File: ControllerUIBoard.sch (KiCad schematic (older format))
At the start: 17 parts

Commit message: [modified:] uln2003 package swap [modified:] Display nomenclature update
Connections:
- net labels added: KeySwitchA, KeySwitchB
- net labels removed: KeyLock.A, KeyLock.B, KeySwitch.A, KeySwitch.B
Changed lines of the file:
@@
 	4700 4850 6400 4850
 Text Label 6400 4450 0    50   ~ 0
-KeySwitch.A
+KeySwitchA
 Text Label 6400 4550 0    50   ~ 0
-KeySwitch.B
+KeySwitchB
 Text Label 6400 3350 0    50   ~ 0
 Signal_Strength_Dial_+
@@
 	1    0    0    -1
 $EndComp
-Text Label 9850 5400 0    50   ~ 0
-KeyLock.A
-Text Label 9850 5500 0    50   ~ 0
-KeyLock.B
 Wire Wire Line
 	9850 5500 9550 5500
@@
 	8850 3650 8600 3650
 Wire Wire Line
-	8700 3750 8850 3750
-Wire Wire Line
 	8850 3850 8600 3850
 Wire Wire Line
 	9350 3850 9600 3850
-Wire Wire Line
-	9600 3750 9350 3750
 Wire Wire Line
 	9600 3550 9350 3550
@@
 Wire Wire Line
 	9350 3650 10700 3650
-Wire Notes Line
-	7600 1850 7600 6000
 Text Notes 7650 2100 0    50   ~ 0
 Spiegelung um Längsachse nätig, je nach Orientierung
@@
 	1    0    0    -1
 $EndComp
-$Comp
-L power:GND #PWR?
-U 1 1 6205CDDF
-P 8700 4150
-AR Path="/6205CDDF" Ref="#PWR?"  Part="1"
-AR Path="/60F87146/6205CDDF" Ref="#PWR?"  Part="1"
-AR Path="/60F18E7A/6205CDDF" Ref="#PWR?"  Part="1"
-F 0 "#PWR?" H 8700 3900 50  0001 C CNN
-F 1 "GND" H 8705 3977 50  0000 C CNN
-F 2 "" H 8700 4150 50  0001 C CNN
-F 3 "" H 8700 4150 50  0001 C CNN
-	1    8700 4150
-	1    0    0    -1
-$EndComp
-Wire Wire Line
-	8700 3750 8700 4150
 Wire Wire Line
 	8550 4600 8550 4900
 Text Notes 6400 3450 0    50   ~ 0
 PWM Output\n
+Text Label 8600 3750 2    50   ~ 0
+OnSwitchLedCathode
+Wire Wire Line
+	8600 3750 8850 3750
+Wire Wire Line
+	10700 3750 10700 3650
+Wire Wire Line
+	9350 3750 10700 3750
+Connection ~ 10700 3650
+Text Label 9850 5400 0    50   ~ 0
+KeySwitchA
+Text Label 9850 5500 0    50   ~ 0
+KeySwitchB
 $EndSCHEMATC

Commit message: - Display Driving abgeschlossen
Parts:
- gave numbers to parts that had none: 17

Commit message: - ATmega überarbeitet - Alle offenen Punkte zusammengefasst
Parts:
- removed C38, C39: 100n, Capacitor_SMD:C_0603_1608Metric, symbol Device:C
- removed J1: ATMEGA_ICSP, Connector_PinHeader_2.54mm:PinHeader_2x03_P2.54mm_Vertical, symbol Connector_Generic:Conn_02x03_Odd_Even
- removed J2: Conn_02x01, Connector_PinHeader_2.54mm:PinHeader_1x02_P2.54mm_Vertical, symbol Connector_Generic:Conn_02x01
- removed J9: Conn_01x03_Male, Connector_PinHeader_2.54mm:PinHeader_1x03_P2.54mm_Vertical, symbol Connector:Conn_01x03_Male
- removed R11, R13, R14, R15, R16, R17: 22k, symbol Device:R
- removed U3: ATmega4809-A, Package_QFP:TQFP-48_7x7mm_P0.5mm, symbol MCU_Microchip_ATmega:ATmega4809-A
- added C77: 4u7/16V/X7R, Capacitor_SMD:C_0805_2012Metric, symbol Device:C
- added C79, C80: 100n/16V/X7R, Capacitor_SMD:C_0603_1608Metric, symbol Device:C
- added J11: SignalStrength, Connector_PinHeader_2.54mm:PinHeader_1x02_P2.54mm_Vertical, symbol Connector_Generic:Conn_01x02
- added J12: KeySwitch, Connector_PinHeader_2.54mm:PinHeader_1x03_P2.54mm_Vertical, symbol Connector_Generic:Conn_01x03
- added J9: ATMEGA_PROG, Connector_PinHeader_2.54mm:PinHeader_1x03_P2.54mm_Vertical, symbol Connector_Generic:Conn_01x03
- added L3: Ferrit/470R/1A/0,2R, Inductor_SMD:L_0603_1608Metric, symbol Device:L
- added R33, R34, R35, R37: 392R/1%, Resistor_SMD:R_0805_2012Metric, symbol Device:R
- added R39, R40, R41, R42, R43, R45: 22k/1%, Resistor_SMD:R_0603_1608Metric, symbol Device:R
- added R44: 100k/5%, Resistor_SMD:R_0603_1608Metric, symbol Device:R
- added U15: ATmega4809-A, Package_QFP:TQFP-48_7x7mm_P0.5mm, symbol TeKaDe:ATmega4809-A
- C78: renamed from C37; value 100n -> 100n/16V/X7R
- R36: renamed from R10; value 22k -> 10k/1%; footprint (none) -> Resistor_SMD:R_0603_1608Metric
- R38: renamed from R12; value 22k -> 22k/1%; footprint (none) -> Resistor_SMD:R_0603_1608Metric
- R46: renamed from R18; footprint (none) -> Resistor_SMD:R_0603_1608Metric
- renumbered J6 to J10
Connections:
- net labels added: LDR, LED_GN, LED_ON, LED_RD, LED_YL, RPI_RUN, UART1_RX, UART1_TX
- net labels removed: LedGreenCathode, LedRedCathode, LedYellowCathode, OnSwitchLedCathode, RPI_RUN_3.3V, UART_RX, UART_TX, UiLdr
- wire segments 92 -> 111
- no-connect marks 15 -> 11
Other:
- note added: "AVCC"
- note added: "BLM18AG471SN1D"
- note added: "PROG"
- note added: "Pin 14/15"
- note added: "Pin 42/43"
- note added: "UI Board:\nLEDs hängen auf 5V ohne Vorwiderstand\nLDR hängt auf 5V"
- note added: "\n\nÄnderungen:\n- Alle Vcc, Gnd Pins von ATmega herausgeführt\n- Bypass Cs angepasst\n- Ferrit für AVcc hinzugefuegt\n- 3 Pin Programmierstecker\n- Pullup für Reset hinzugefügt\n- Spannungsteiler R für LDR auf 10k geändet (typ.)\n- LED Vorwiderstande (ATmega min. 100mA / Pingroup)\n -> Vorwiderstände auf ca 10mA auslegen\n"
- note removed: "Empfehlung zur Kompatibilität:\nhttps://microchipdeveloper.com/atmelice:updi"
- note removed: "PWM Output\n"
- moved on the sheet: C78, J10, R36, R38, R46

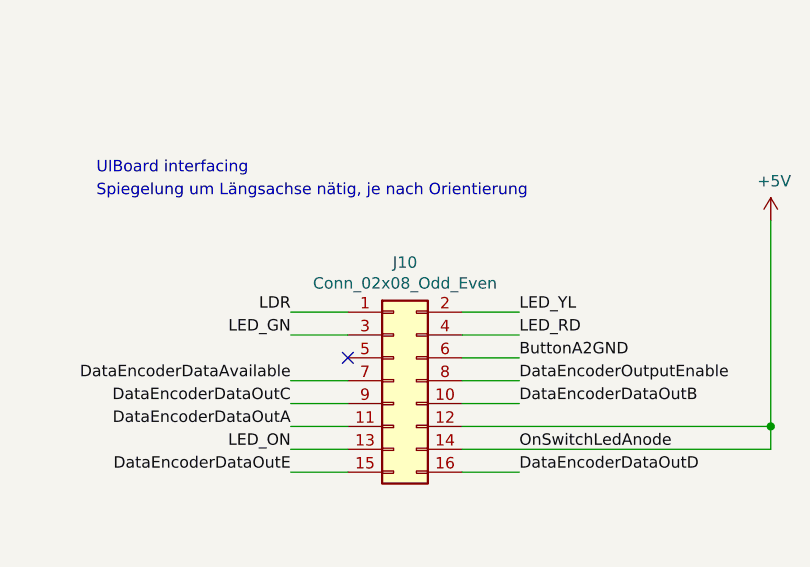
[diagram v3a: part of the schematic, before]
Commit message: - Platzoptimierungen
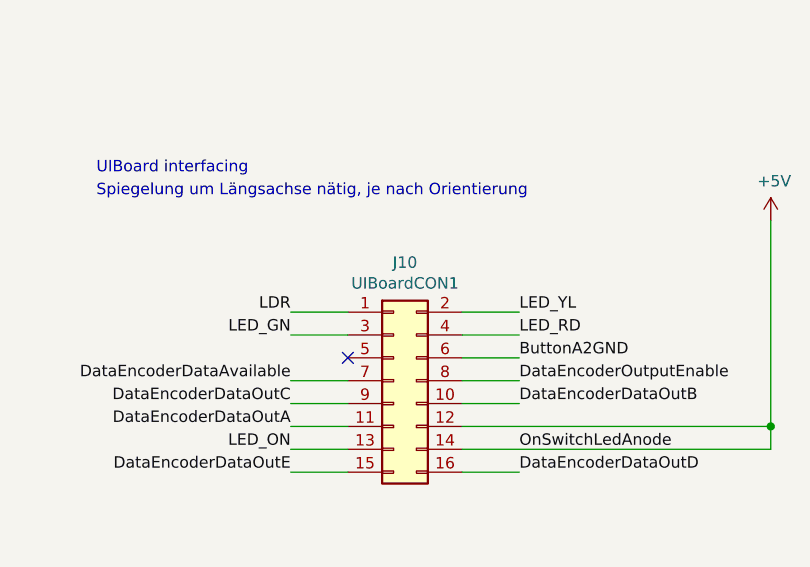
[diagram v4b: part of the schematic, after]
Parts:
- C78, C79, C80: footprint Capacitor_SMD:C_0603_1608Metric -> Capacitor_SMD:C_0402_1005Metric
- J10: value Conn_02x08_Odd_Even -> UIBoardCON1
- R38, R39, R40, R41, R42, R43, R44, R45, R46: footprint Resistor_SMD:R_0603_1608Metric -> Resistor_SMD:R_0402_1005Metric
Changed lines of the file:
@@
 F 0 "C78" H 1915 6996 50  0000 L CNN
 F 1 "100n/16V/X7R" H 1915 6905 50  0000 L CNN
-F 2 "Capacitor_SMD:C_0603_1608Metric" H 1838 6800 50  0001 C CNN
+F 2 "Capacitor_SMD:C_0402_1005Metric" H 1838 6800 50  0001 C CNN
 F 3 "~" H 1800 6950 50  0001 C CNN
 	1    1800 6950
@@
 F 0 "R38" H 2970 4246 50  0000 L CNN
 F 1 "22k/1%" H 2970 4155 50  0000 L CNN
-F 2 "Resistor_SMD:R_0603_1608Metric" V 2830 4200 50  0001 C CNN
+F 2 "Resistor_SMD:R_0402_1005Metric" V 2830 4200 50  0001 C CNN
 F 3 "~" H 2900 4200 50  0001 C CNN
 	1    2900 4200
@@
 $EndComp
 $Comp
-L power:GND #PWR0171
+L power:GND #PWR0173
 U 1 1 60F96DE0
 P 2900 5050
-F 0 "#PWR0171" H 2900 4800 50  0001 C CNN
+F 0 "#PWR0173" H 2900 4800 50  0001 C CNN
 F 1 "GND" H 2905 4877 50  0000 C CNN
 F 2 "" H 2900 5050 50  0001 C CNN
@@
 	2900 4350 2900 5050
 $Comp
-L power:GND #PWR0172
+L power:GND #PWR0174
 U 1 1 60FB5234
 P 3100 5050
-F 0 "#PWR0172" H 3100 4800 50  0001 C CNN
+F 0 "#PWR0174" H 3100 4800 50  0001 C CNN
 F 1 "GND" H 3105 4877 50  0000 C CNN
 F 2 "" H 3100 5050 50  0001 C CNN
@@
 	3100 4700 3100 5050
 $Comp
-L power:GND #PWR0174
+L power:GND #PWR0176
 U 1 1 60FC9499
 P 3300 5050
-F 0 "#PWR0174" H 3300 4800 50  0001 C CNN
+F 0 "#PWR0176" H 3300 4800 50  0001 C CNN
 F 1 "GND" H 3305 4877 50  0000 C CNN
 F 2 "" H 3300 5050 50  0001 C CNN
@@
 	3700 4700 3700 5050
 $Comp
-L power:+5V #PWR0173
+L power:+5V #PWR0175
 U 1 1 6102E230
 P 3300 950
-F 0 "#PWR0173" H 3300 800 50  0001 C CNN
+F 0 "#PWR0175" H 3300 800 50  0001 C CNN
 F 1 "+5V" H 3315 1123 50  0000 C CNN
 F 2 "" H 3300 950 50  0001 C CNN
@@
 F 0 "R46" V 5693 1750 50  0000 C CNN
 F 1 "10k" V 5784 1750 50  0000 C CNN
-F 2 "Resistor_SMD:R_0603_1608Metric" V 5830 1750 50  0001 C CNN
+F 2 "Resistor_SMD:R_0402_1005Metric" V 5830 1750 50  0001 C CNN
 F 3 "~" H 5900 1750 50  0001 C CNN
 	1    5900 1750
@@
 	1800 7100 1800 7300
 $Comp
-L power:+5V #PWR0175
+L power:+5V #PWR0171
 U 1 1 6118A64F
 P 2800 6600
-F 0 "#PWR0175" H 2800 6450 50  0001 C CNN
+F 0 "#PWR0171" H 2800 6450 50  0001 C CNN
 F 1 "+5V" H 2815 6773 50  0000 C CNN
 F 2 "" H 2800 6600 50  0001 C CNN
@@
 $EndComp
 $Comp
-L power:GND #PWR0176
+L power:GND #PWR0172
 U 1 1 6118A655
 P 2800 7300
-F 0 "#PWR0176" H 2800 7050 50  0001 C CNN
+F 0 "#PWR0172" H 2800 7050 50  0001 C CNN
 F 1 "GND" H 2805 7127 50  0000 C CNN
 F 2 "" H 2800 7300 50  0001 C CNN
@@
 	2800 7100 2800 7300
 $Comp
-L power:+5V #PWR0181
+L power:+5V #PWR0180
 U 1 1 6118CFCA
 P 3800 6550
-F 0 "#PWR0181" H 3800 6400 50  0001 C CNN
+F 0 "#PWR0180" H 3800 6400 50  0001 C CNN
 F 1 "+5V" H 3815 6723 50  0000 C CNN
 F 2 "" H 3800 6550 50  0001 C CNN
@@
 $EndComp
 $Comp
-L power:GND #PWR0182
+L power:GND #PWR0181
 U 1 1 6118CFD0
 P 3800 7300
-F 0 "#PWR0182" H 3800 7050 50  0001 C CNN
+F 0 "#PWR0181" H 3800 7050 50  0001 C CNN
 F 1 "GND" H 3805 7127 50  0000 C CNN
 F 2 "" H 3800 7300 50  0001 C CNN
@@
 AR Path="/60F18E7A/6205CD91" Ref="J10"  Part="1"
 F 0 "J10" H 9050 4667 50  0000 C CNN
-F 1 "Conn_02x08_Odd_Even" H 9050 4576 50  0000 C CNN
+F 1 "UIBoardCON1" H 9050 4576 50  0000 C CNN
 F 2 "Connector_PinSocket_2.54mm:PinSocket_2x08_P2.54mm_Vertical" H 9000 4150 50  0001 C CNN
 F 3 "~" H 9000 4150 50  0001 C CNN
@@
 F 0 "C79" H 2915 6996 50  0000 L CNN
 F 1 "100n/16V/X7R" H 2915 6905 50  0000 L CNN
-F 2 "Capacitor_SMD:C_0603_1608Metric" H 2838 6800 50  0001 C CNN
+F 2 "Capacitor_SMD:C_0402_1005Metric" H 2838 6800 50  0001 C CNN
 F 3 "~" H 2800 6950 50  0001 C CNN
 	1    2800 6950
@@
 F 0 "C80" H 3915 7146 50  0000 L CNN
 F 1 "100n/16V/X7R" H 3915 7055 50  0000 L CNN
-F 2 "Capacitor_SMD:C_0603_1608Metric" H 3838 6950 50  0001 C CNN
+F 2 "Capacitor_SMD:C_0402_1005Metric" H 3838 6950 50  0001 C CNN
 F 3 "~" H 3800 7100 50  0001 C CNN
 	1    3800 7100
@@
 AVCC
 $Comp
-L power:GND #PWR0180
+L power:GND #PWR0182
 U 1 1 60FD580F
 P 3900 5050
-F 0 "#PWR0180" H 3900 4800 50  0001 C CNN
+F 0 "#PWR0182" H 3900 4800 50  0001 C CNN
 F 1 "GND" H 3905 4877 50  0000 C CNN
 F 2 "" H 3900 5050 50  0001 C CNN
@@
 F 0 "R39" H 3170 4596 50  0000 L CNN
 F 1 "22k/1%" H 3170 4505 50  0000 L CNN
-F 2 "Resistor_SMD:R_0603_1608Metric" V 3030 4550 50  0001 C CNN
+F 2 "Resistor_SMD:R_0402_1005Metric" V 3030 4550 50  0001 C CNN
 F 3 "~" H 3100 4550 50  0001 C CNN
 	1    3100 4550
@@
 F 0 "R41" H 3370 4946 50  0000 L CNN
 F 1 "22k/1%" H 3370 4855 50  0000 L CNN
-F 2 "Resistor_SMD:R_0603_1608Metric" V 3230 4900 50  0001 C CNN
+F 2 "Resistor_SMD:R_0402_1005Metric" V 3230 4900 50  0001 C CNN
 F 3 "~" H 3300 4900 50  0001 C CNN
 	1    3300 4900
@@
 F 0 "R42" H 3570 4246 50  0000 L CNN
 F 1 "22k/1%" H 3570 4155 50  0000 L CNN
-F 2 "Resistor_SMD:R_0603_1608Metric" V 3430 4200 50  0001 C CNN
+F 2 "Resistor_SMD:R_0402_1005Metric" V 3430 4200 50  0001 C CNN
 F 3 "~" H 3500 4200 50  0001 C CNN
 	1    3500 4200
@@
 F 0 "R43" H 3770 4596 50  0000 L CNN
 F 1 "22k/1%" H 3770 4505 50  0000 L CNN
-F 2 "Resistor_SMD:R_0603_1608Metric" V 3630 4550 50  0001 C CNN
+F 2 "Resistor_SMD:R_0402_1005Metric" V 3630 4550 50  0001 C CNN
 F 3 "~" H 3700 4550 50  0001 C CNN
 	1    3700 4550
@@
 F 0 "R45" H 3970 4946 50  0000 L CNN
 F 1 "22k/1%" H 3970 4855 50  0000 L CNN
-F 2 "Resistor_SMD:R_0603_1608Metric" V 3830 4900 50  0001 C CNN
+F 2 "Resistor_SMD:R_0402_1005Metric" V 3830 4900 50  0001 C CNN
 F 3 "~" H 3900 4900 50  0001 C CNN
 	1    3900 4900
@@
 F 0 "R44" H 3870 1296 50  0000 L CNN
 F 1 "100k/5%" H 3870 1205 50  0000 L CNN
-F 2 "Resistor_SMD:R_0603_1608Metric" V 3730 1250 50  0001 C CNN
+F 2 "Resistor_SMD:R_0402_1005Metric" V 3730 1250 50  0001 C CNN
 F 3 "~" H 3800 1250 50  0001 C CNN
 	1    3800 1250
@@
 F 0 "R40" H 3370 1296 50  0000 L CNN
 F 1 "22k/1%" H 3370 1205 50  0000 L CNN
-F 2 "Resistor_SMD:R_0603_1608Metric" V 3230 1250 50  0001 C CNN
+F 2 "Resistor_SMD:R_0402_1005Metric" V 3230 1250 50  0001 C CNN
 F 3 "~" H 3300 1250 50  0001 C CNN
 	1    3300 1250

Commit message: [fix:] general troublespots -> notes
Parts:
- R46: value 10k -> 15k
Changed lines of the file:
@@
 $Descr A4 11693 8268
 encoding utf-8
-Sheet 9 9
+Sheet 2 9
 Title ""
 Date ""
@@
 P 5900 1750
 F 0 "R46" V 5693 1750 50  0000 C CNN
-F 1 "10k" V 5784 1750 50  0000 C CNN
+F 1 "15k" V 5784 1750 50  0000 C CNN
 F 2 "Resistor_SMD:R_0402_1005Metric" V 5830 1750 50  0001 C CNN
 F 3 "~" H 5900 1750 50  0001 C CNN
@@
 Wire Wire Line
 	5300 1650 6350 1650
-Text Label 1600 2350 2    50   ~ 0
-ButtonA2GND
 $Comp
 L power:+5V #PWR0168
@@
 Wire Wire Line
 	1600 3250 2500 3250
-Wire Wire Line
-	1600 2350 3300 2350
-Wire Wire Line
-	3300 1400 3300 2350
-Connection ~ 3300 2350
-Wire Wire Line
-	3300 2350 4100 2350
 $Comp
 L Device:R R36
@@
 NoConn ~ 5300 3450
 NoConn ~ 5300 3550
-NoConn ~ 4100 2250
 Wire Wire Line
 	4100 1650 1600 1650
@@
 	0    1    1    0
 $EndComp
+Text Label 1600 2350 2    50   ~ 0
+ButtonA2GND
+Wire Wire Line
+	1600 2350 3300 2350
+Connection ~ 3300 2350
+Wire Wire Line
+	3300 1400 3300 2350
+Wire Wire Line
+	3300 2350 4100 2350
+NoConn ~ 4100 2250
 $EndSCHEMATC

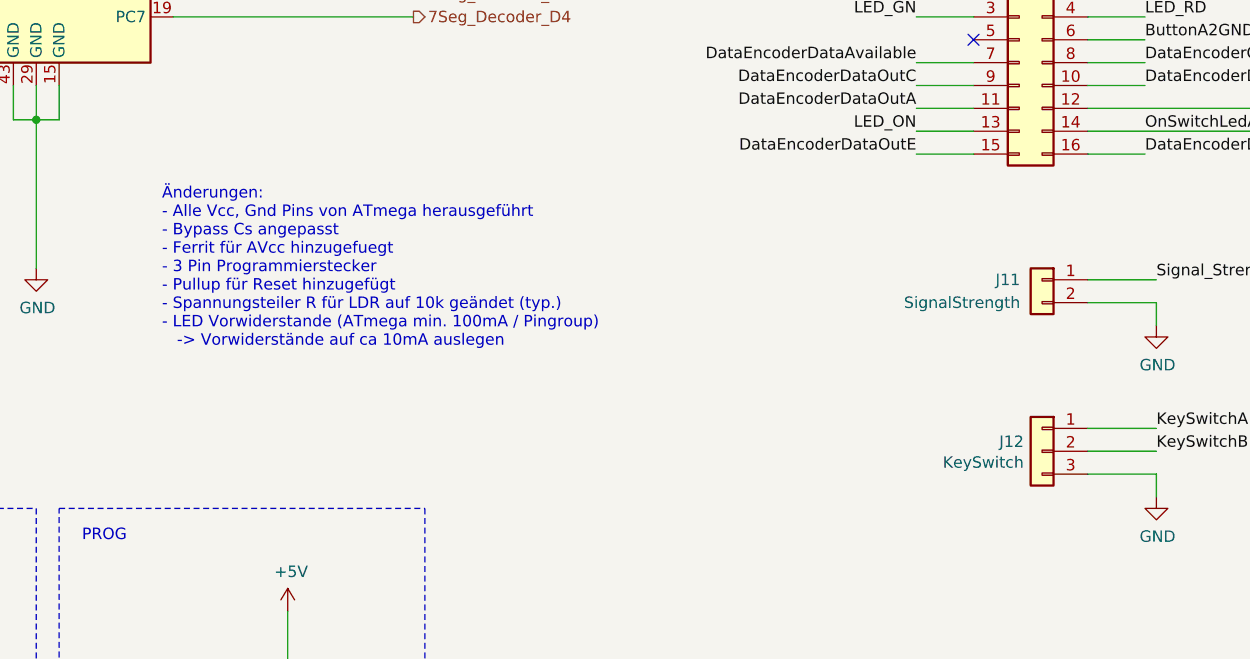
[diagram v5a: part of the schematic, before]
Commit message: [mod:] Note updates, KeySwitch mechanical definition
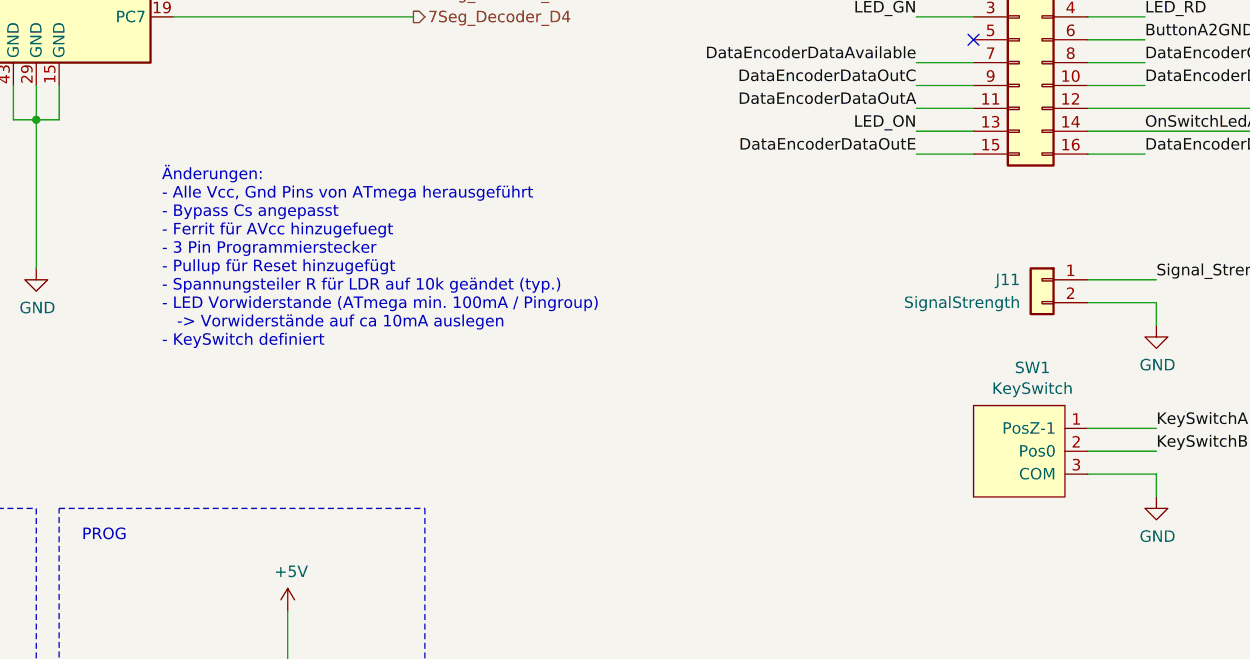
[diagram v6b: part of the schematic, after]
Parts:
- removed J12: KeySwitch, Connector_PinHeader_2.54mm:PinHeader_1x03_P2.54mm_Vertical, symbol Connector_Generic:Conn_01x03
- added SW1: KeySwitch, TeKaDe:KeySwitch, symbol TeKaDe:KeySwitch
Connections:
- net GND: now also SW1.3 (COM)
- net KeySwitchA: now also SW1.1 (PosZ-1)
- net KeySwitchB: now also SW1.2 (Pos0)
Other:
- note added: "\n\nÄnderungen:\n- Alle Vcc, Gnd Pins von ATmega herausgeführt\n- Bypass Cs angepasst\n- Ferrit für AVcc hinzugefuegt\n- 3 Pin Programmierstecker\n- Pullup für Reset hinzugefügt\n- Spannungsteiler R für LDR auf 10k geändet (typ.)\n- LED Vorwiderstande (ATmega min. 100mA / Pingroup)\n -> Vorwiderstände auf ca 10mA auslegen\n- KeySwitch definiert"
- note removed: "\n\nÄnderungen:\n- Alle Vcc, Gnd Pins von ATmega herausgeführt\n- Bypass Cs angepasst\n- Ferrit für AVcc hinzugefuegt\n- 3 Pin Programmierstecker\n- Pullup für Reset hinzugefügt\n- Spannungsteiler R für LDR auf 10k geändet (typ.)\n- LED Vorwiderstande (ATmega min. 100mA / Pingroup)\n -> Vorwiderstände auf ca 10mA auslegen\n"
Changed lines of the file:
@@
 	4850 1100 4850 1450
 Text Notes 5250 5400 0    50   ~ 0
-\n\nÄnderungen:\n- Alle Vcc, Gnd Pins von ATmega herausgeführt\n- Bypass Cs angepasst\n- Ferrit für AVcc hinzugefuegt\n- 3 Pin Programmierstecker\n- Pullup für Reset hinzugefügt\n- Spannungsteiler R für LDR auf 10k geändet (typ.)\n- LED Vorwiderstande (ATmega min. 100mA / Pingroup)\n   -> Vorwiderstände auf ca 10mA auslegen\n
+\n\nÄnderungen:\n- Alle Vcc, Gnd Pins von ATmega herausgeführt\n- Bypass Cs angepasst\n- Ferrit für AVcc hinzugefuegt\n- 3 Pin Programmierstecker\n- Pullup für Reset hinzugefügt\n- Spannungsteiler R für LDR auf 10k geändet (typ.)\n- LED Vorwiderstande (ATmega min. 100mA / Pingroup)\n   -> Vorwiderstände auf ca 10mA auslegen\n- KeySwitch definiert
 $Comp
 L Device:C C?
@@
 F 3 "~" H 5500 6950 50  0001 C CNN
 	1    5500 6950
-	-1   0    0    -1
-$EndComp
-$Comp
-L Connector_Generic:Conn_01x03 J12
-U 1 1 60FFA72C
-P 9100 5850
-F 0 "J12" H 9180 5892 50  0000 L CNN
-F 1 "KeySwitch" H 9180 5801 50  0000 L CNN
-F 2 "Connector_PinHeader_2.54mm:PinHeader_1x03_P2.54mm_Vertical" H 9100 5850 50  0001 C CNN
-F 3 "~" H 9100 5850 50  0001 C CNN
-	1    9100 5850
 	-1   0    0    -1
 $EndComp
@@
 	3300 2350 4100 2350
 NoConn ~ 4100 2250
+$Comp
+L TeKaDe:KeySwitch SW1
+U 1 1 614FE351
+P 9300 5750
+F 0 "SW1" H 9058 6015 50  0000 C CNN
+F 1 "KeySwitch" H 9058 5924 50  0000 C CNN
+F 2 "TeKaDe:KeySwitch" H 9350 6200 50  0001 C CNN
+F 3 "" H 9250 5500 50  0001 C CNN
+	1    9300 5750
+	1    0    0    -1
+$EndComp
 $EndSCHEMATC
